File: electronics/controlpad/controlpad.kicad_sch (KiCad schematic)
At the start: 14 parts, among them J1 USB - Host, SW1 START, SW10 1, SW2 2, SW3 3, SW4 4, SW5 5, SW6 6, SW7 7, SW8 8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

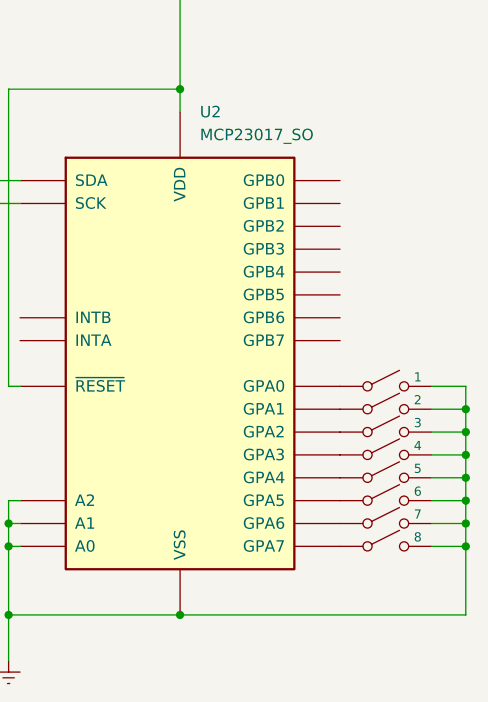
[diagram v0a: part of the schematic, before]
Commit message: Adding to schematics all buttons on GPIO-B (8-15)
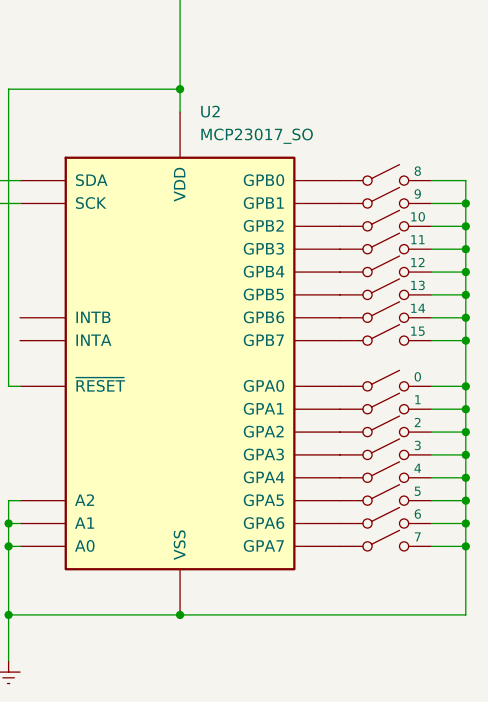
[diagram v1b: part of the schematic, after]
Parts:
- added SW11: 8, symbol Switch:SW_DPST_x2
- added SW12: 10, symbol Switch:SW_DPST_x2
- added SW13: 11, symbol Switch:SW_DPST_x2
- added SW14: 12, symbol Switch:SW_DPST_x2
- added SW15: 13, symbol Switch:SW_DPST_x2
- added SW16: 14, symbol Switch:SW_DPST_x2
- added SW17: 15, symbol Switch:SW_DPST_x2
- added SW9: 9, symbol Switch:SW_DPST_x2
- SW10: value 1 -> 0
- SW2: value 2 -> 1
- SW3: value 3 -> 2
- SW4: value 4 -> 3
- SW5: value 5 -> 4
- SW6: value 6 -> 5
- SW7: value 7 -> 6
- SW8: value 8 -> 7
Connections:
- net GNDREF: now also SW11.2 (B), SW12.2 (B), SW13.2 (B), SW14.2 (B), SW15.2 (B), SW16.2 (B), SW17.2 (B), SW9.2 (B)
- net at U2.1 (GPB0): now also SW11.1 (A)
- net at U2.2 (GPB1): now also SW9.1 (A)
- net at U2.3 (GPB2): now also SW12.1 (A)
- net at U2.4 (GPB3): now also SW13.1 (A)
- net at U2.5 (GPB4): now also SW14.1 (A)
- net at U2.6 (GPB5): now also SW15.1 (A)
- net at U2.7 (GPB6): now also SW16.1 (A)
- net at U2.8 (GPB7): now also SW17.1 (A)

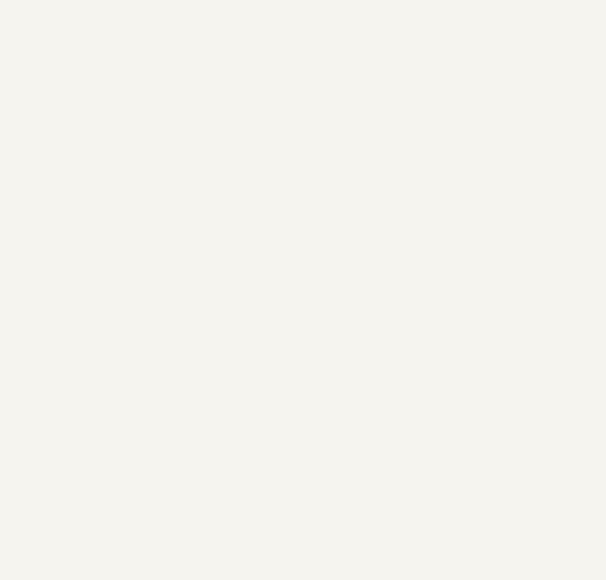
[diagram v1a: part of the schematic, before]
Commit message: Adding display to the board
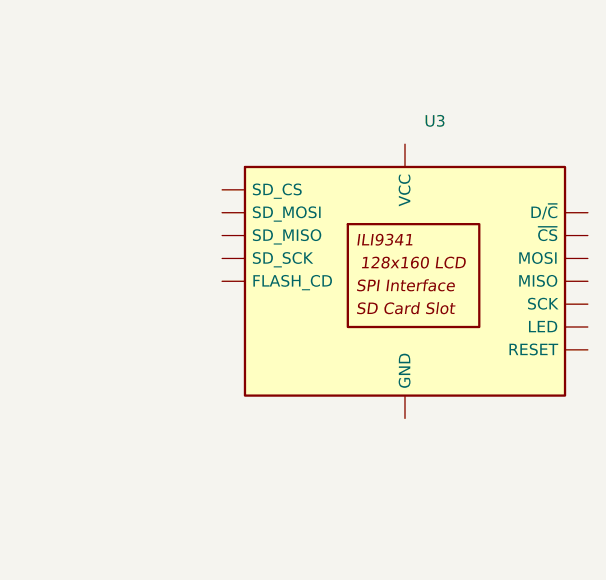
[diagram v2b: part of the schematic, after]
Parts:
- added U3: CR2013-MI2120, Display:CR2013-MI2120, symbol Driver_Display:CR2013-MI2120
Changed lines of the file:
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@@
+			"AAAAAAAAAAAAAAAAAAAAAAAAAAAAAAAAAAAAAAAAAAAAAAAAAAAAAAAAAAAAAAAAAAAAAAAAAAAA"
+			"AAAAAAAAAAAAAAAAAAAAAAAAAAAAAAAAAAAAAAAAAAAAAAAAAAAAAAAAAAAAAAAAAAAAAAAAAAAA"
+			"AAAAAAAAAAAAAAAAAAAAAAAAAAAAAAAAAAAAAAAAAAAAAAAAAAAAAAAAAAAAAAAAAAAAAAAAAAAA"
+			"AAAAAAAAAAAAAAAAAAAAAAAAAAAAAAAAAAAAAAAAAAAAAAAAAAAAAAAAAAAAAAAAAAAAAAAAAAAA"
+			"AAAAAAAAAAAAAAAAAAAAAAAAAAAAAAAAAAAAAAAAAAAAAAAAAAAAAAAAAAAAAAAAAAAAAAAAAAAA"
+			"AAAAAAAAAAAAAAAAAAAAAAAAAAAAAAAAAAAAAAAAAAAAAAAAAAAAAAAAAAAAAAAAAAAAAAAAAAAA"
+			"AAAAAAAAAAAAAAAAAAAAAAAAAAAAAAAAAAAAAAAAAAAAAAAAAAAAAAAAAAAAAAAAAAAAAAAAAAAA"
+			"AAAAAAAAAAAAAAAAAAAAAAAAAAAAAAAAAAAAAAAAAAAAAAAAAAAAAAAAAAAAAAAAAAAAAAAAAAAA"
+			"AAAAAAAAAAAAAAAAAAAAAAAAAAAAAAAAAAAAAAAAAAAAAAAAAAAAAAAAAAAAAAAAAAAAAAAAAAAA"
+			"AAAAAAAAAAAAAAAAAAAAAAAAAAAAAAAAAAAAAAAAAAAAAAAAAAAAAAAAAAAAAAAAAAAAAAAAAAAA"
+			"AAAAAAAAAAAAAAAAAAAAAAAAAAAAAAAAAAAAAAAAAAAAAAAAAAAAAAAAAAAAAAAAAAAAAAAAAAAA"
+			"AAAAAAAAAAAAAAAAAAAAAAAAAAAAAAAAAAAAAAAAAAAAAAAAAAAAAAAAAAAAAAAAAAAAAAAAAAAA"
+			"AAAAAAAAAAAAAAAAAAAAAAAAAAAAAAAAAAAAAAAAAAAAAAAAAAAAAAAAAAAAAAAAAAAAAAAAAAAA"
+			"AAAAAAAAAAAAAAAAAAAAAAAAAAAAAAAAAAAAAAAAAAAAAAAAAAAAAAAAAAAAAAAAAAAAAAAAAAAA"
+			"AAAAAAAAAAAAAAAAAAAAAAAAAAAAAAAAAAAAAAAAAAAAAAAAAAAAAAAAAAAAAAAAAAAAAAAAAAAA"
+			"AAAAAAAAAAAAAAAAAAAAAAAAAAAAAAAAAAAAAAAAAAAAAAAAAAAAAAAAAAAAAAAAAAAAAAAAAAAA"
+			"AAAAAAAAAAAAAAAAAAAAAAAAAAAAAAAAAAAAAAAAAAAAAAAAAAAAAAAAAAAAAAAAAAAAAAAAAAAA"
+			"AAAAAAAAAAAAAAAAAAAAAAAAAAAAAAAAAAAAAAAAAAAAAAAAAAAAAAAAAAAAAAAAAAAAAAAAAAAA"
 			"AAAAAAAAAAAAAAAAAAAAAAAAAAAAAAAAAAAAAAAAAAAAAAAAAAAAAAAAAAAAAAAAAAAAAAAAAAAA"
 			"AAAAAAAAAAAAAAAAAAAAAAAAAAAAAAAAAAAAAAAAAAAAAAAAAAAAAAAAAAAAAAAAAAAAAAAAAAAA"
@@
 					(unit 1)
 				)
+			)
+		)
+	)
+	(symbol
+		(lib_id "Driver_Display:CR2013-MI2120")
+		(at 210.82 53.34 0)
+		(unit 1)
+		(exclude_from_sim no)
+		(in_bom yes)
+		(on_board yes)
+		(dnp no)
+		(fields_autoplaced yes)
+		(property "Reference" "U3"
+			(at 212.9633 35.56 0)
+			(effects
+				(font
+					(size 1.27 1.27)
+				)
+				(justify left)
+			)
+		)
+		(property "Value" "CR2013-MI2120"
+			(at 212.9633 38.1 0)
+			(effects
+				(font
+					(size 1.27 1.27)
+				)
+				(justify left)
+				(hide yes)
+			)
+		)
+		(property "Footprint" "Display:CR2013-MI2120"
+			(at 210.82 71.12 0)
+			(effects
+				(font
+					(size 1.27 1.27)
+				)
+				(hide yes)
+			)
+		)
+		(property "Datasheet" "http://pan.baidu.com/s/11Y990"
+			(at 194.31 40.64 0)
+			(effects
+				(font
+					(size 1.27 1.27)
+				)
+				(hide yes)
+			)
+		)
+		(property "Description" "ILI9341 controller, SPI TFT LCD Display, 9-pin breakout PCB, 4-pin SD card interface, 5V/3.3V"
+			(at 210.82 53.34 0)
+			(effects
+				(font
+					(size 1.27 1.27)
+				)
+				(hide yes)
+			)
+		)
+		(pin "7"
+		)
+		(pin "10"
+		)
+		(pin "13"
+		)
+		(pin "12"
+		)
+		(pin "11"
+		)
+		(pin "8"
+		)
+		(pin "3"
+		)
+		(pin "9"
+		)
+		(pin "14"
+		)
+		(pin "5"
+		)
+		(pin "1"
+		)
+		(pin "6"
+		)
+		(pin "4"
+		)
+		(pin "2"
+		)
+		(instances
+			(project ""
+				(path "/c06f4dac-aef6-4417-a281-a2a0987c6210"
+					(reference "U3")
+					(unit 1)
+				)

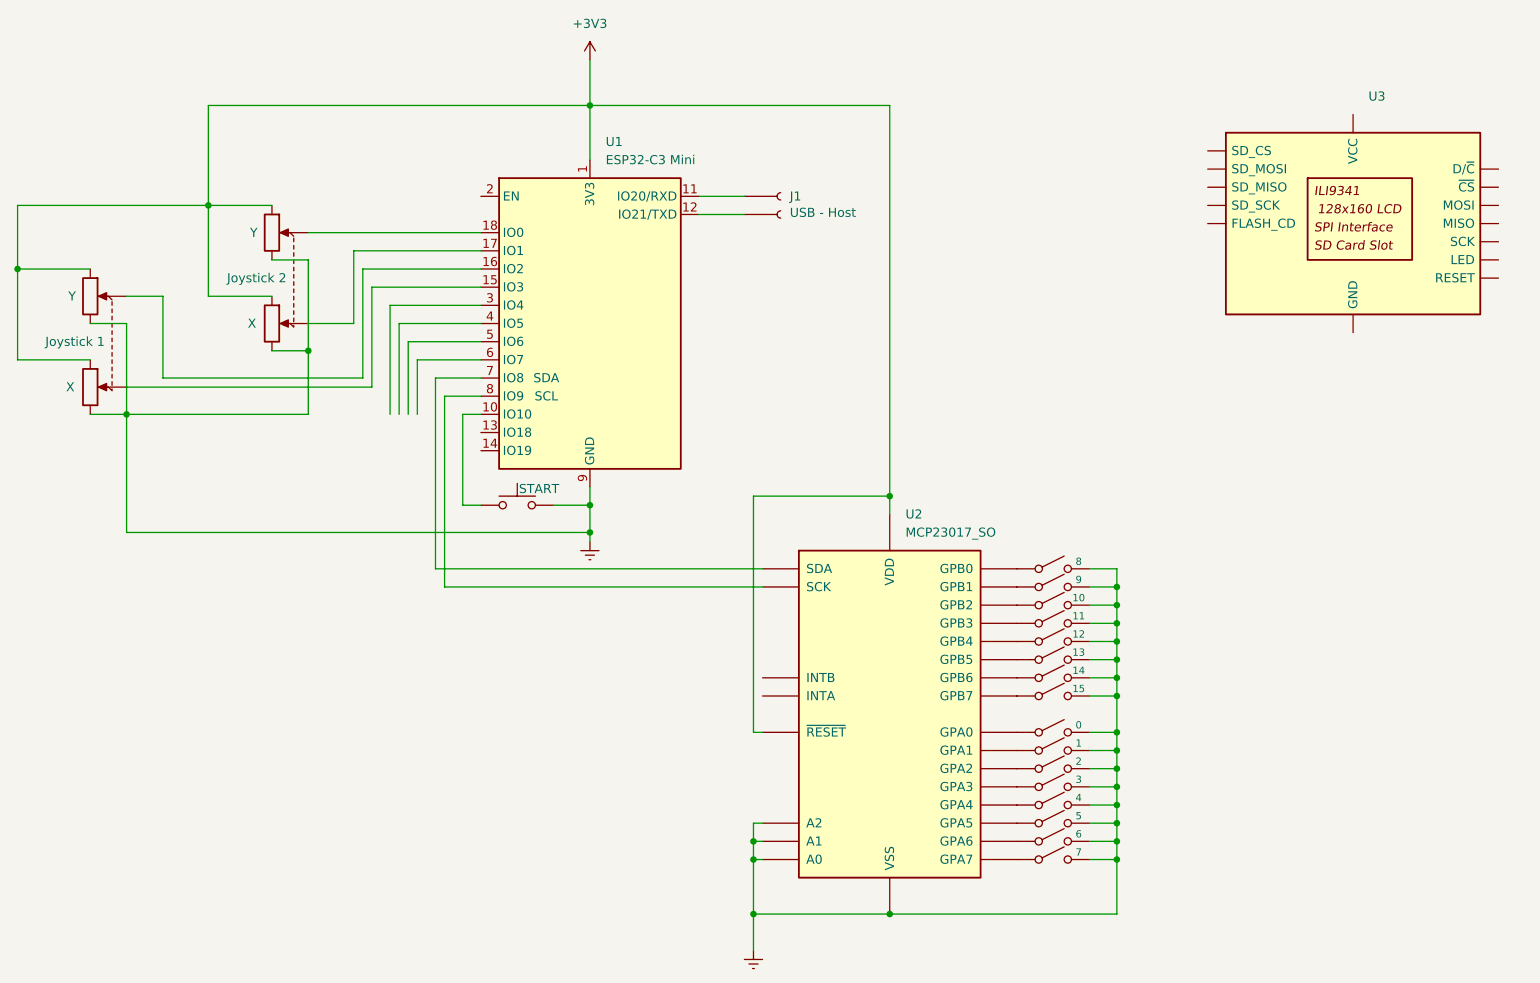
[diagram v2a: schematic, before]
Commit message: display 3v3 and gnd
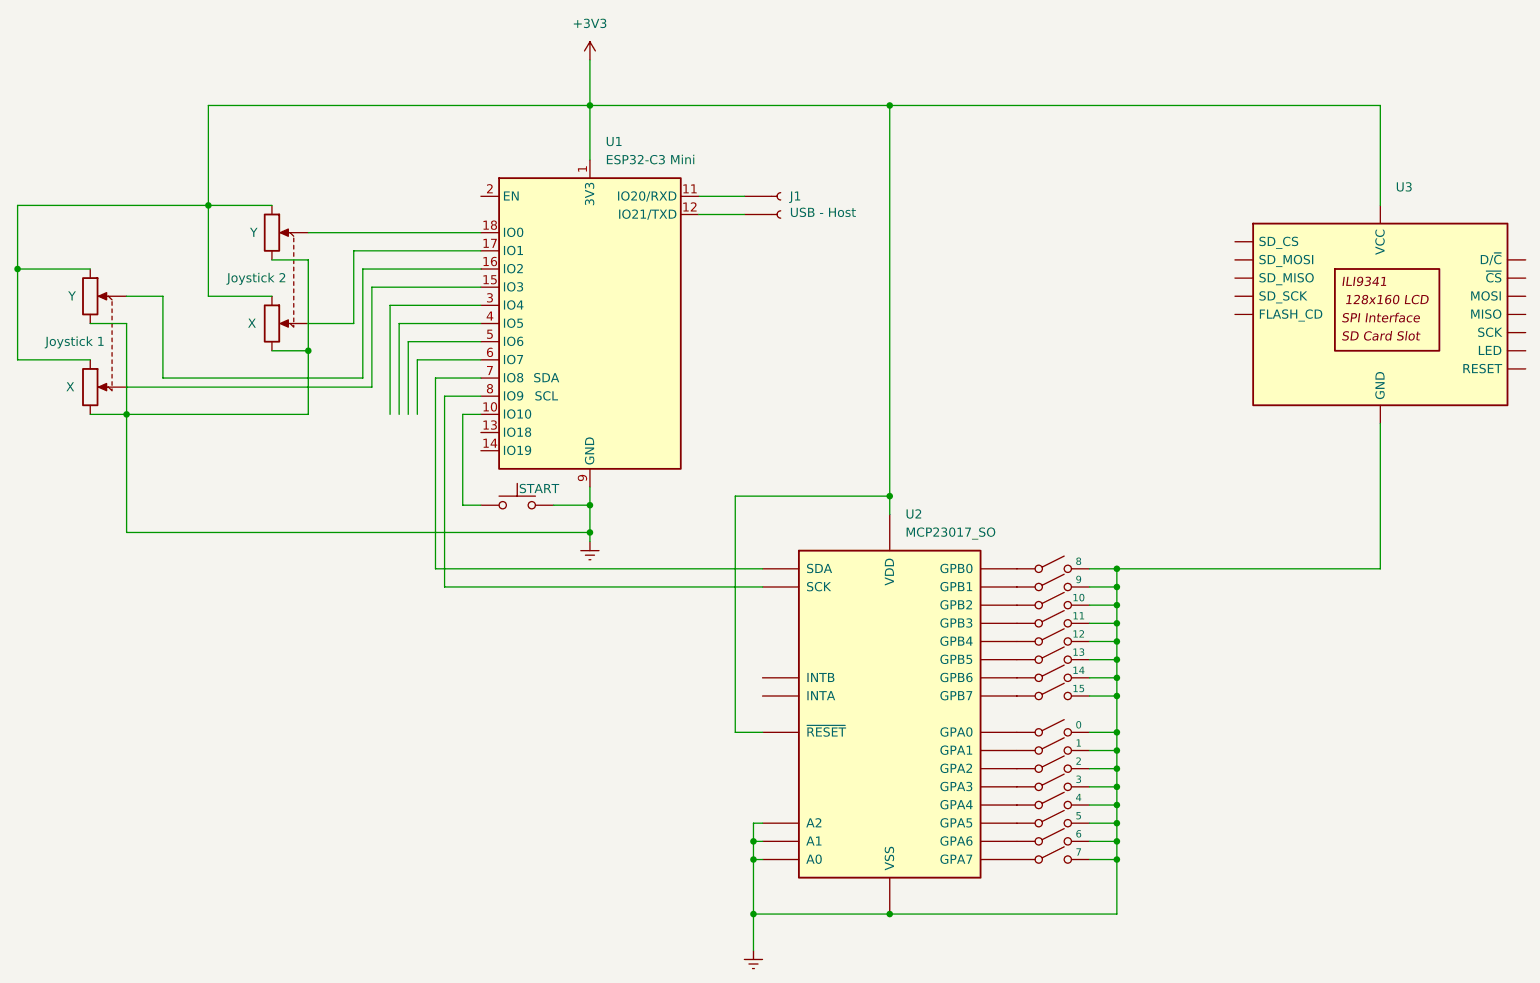
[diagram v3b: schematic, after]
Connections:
- net +3V3: now also U3.1 (VCC)
- net GNDREF: now also U3.2 (GND)
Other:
- moved on the sheet: U3

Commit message: adding resistor on LED pin
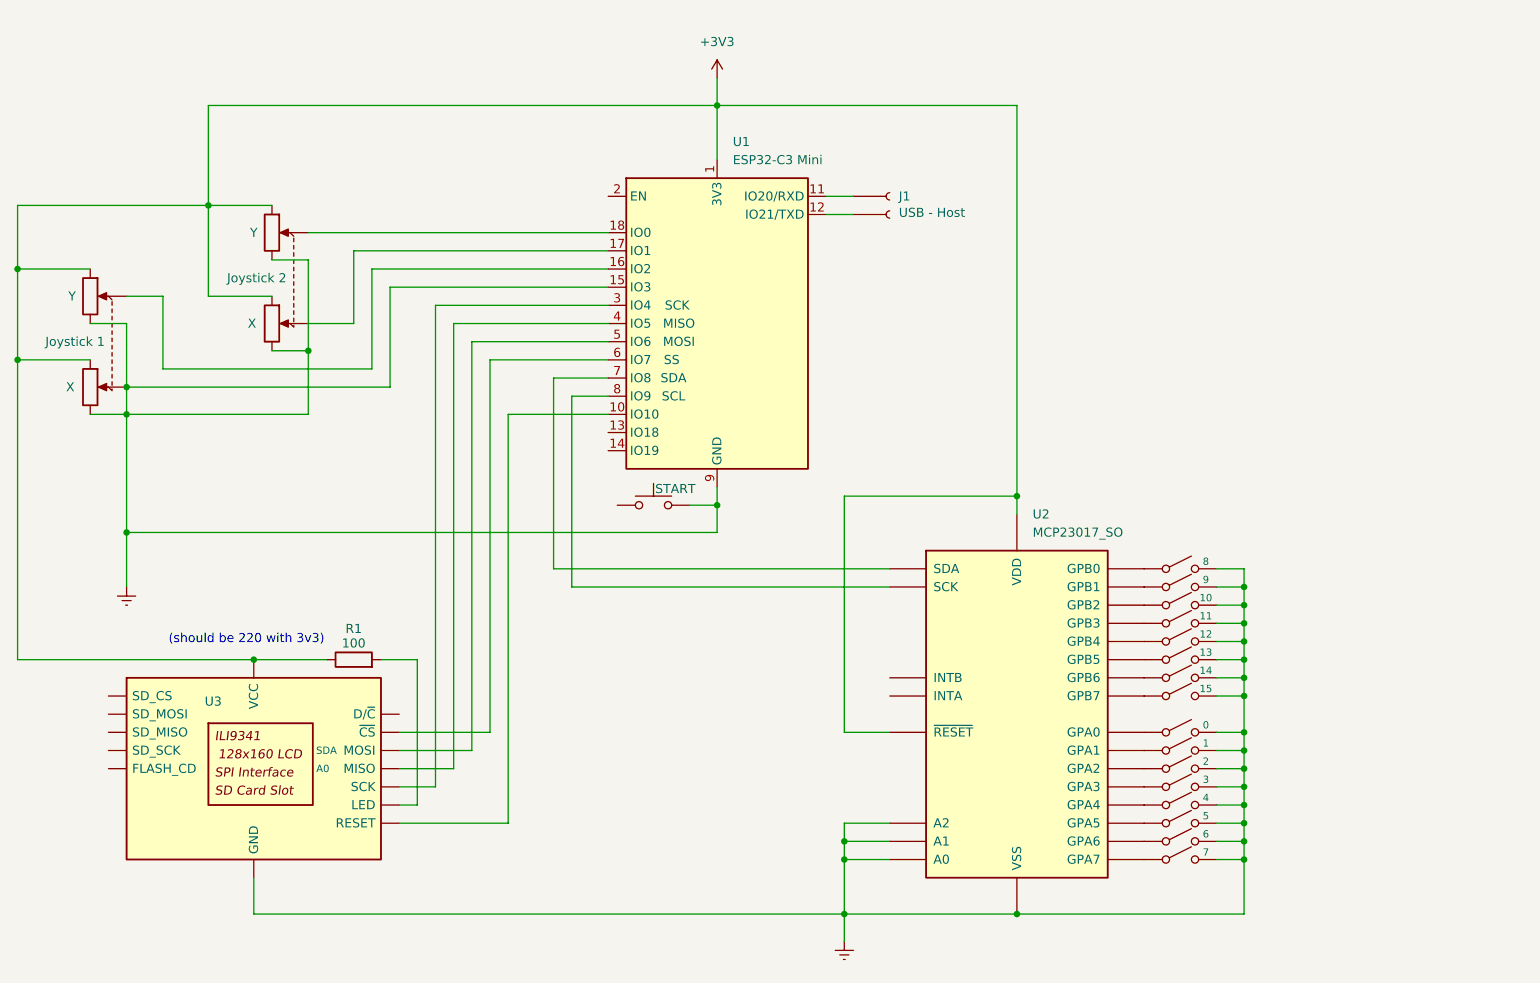
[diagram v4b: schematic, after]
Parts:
- added R1: 100, symbol Device:R
- U1: Field10 (none) -> SS; Field7 (none) -> SCK; Field8 (none) -> MISO; Field9 (none) -> MOSI
- U3: A0 (none) -> A0; MOSI (none) -> SDA
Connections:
- net +3V3: now also R1.1
- net GNDREF: now also RV2.5, U1.15 (IO3)
- net at U3.3 (~{CS}): now also U1.6 (IO7)
- net at U3.4 (RESET): now also U1.10 (IO10)
- net at U3.6 (MOSI): now also U1.5 (IO6)
- net at U3.7 (SCK): now also U1.3 (IO4)
- net at U3.8 (LED): now also R1.2
- net at U3.9 (MISO): now also U1.4 (IO5)
- net at SW1.1: no longer U1.10 (IO10)
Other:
- note added: "(should be 220 with 3v3)"
- moved on the sheet: J1, U1, U2, U3
